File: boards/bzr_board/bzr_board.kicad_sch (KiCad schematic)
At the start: 13 parts, among them J1 Conn_01x06, U1 74HC00

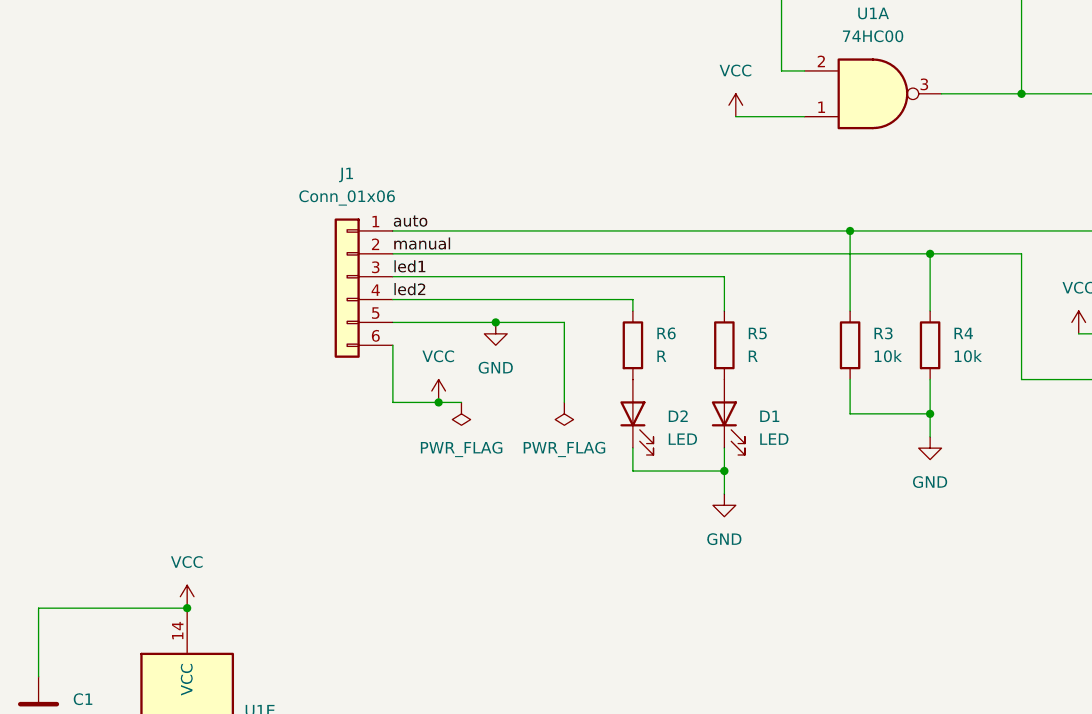
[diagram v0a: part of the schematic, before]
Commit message: set LED and resistors
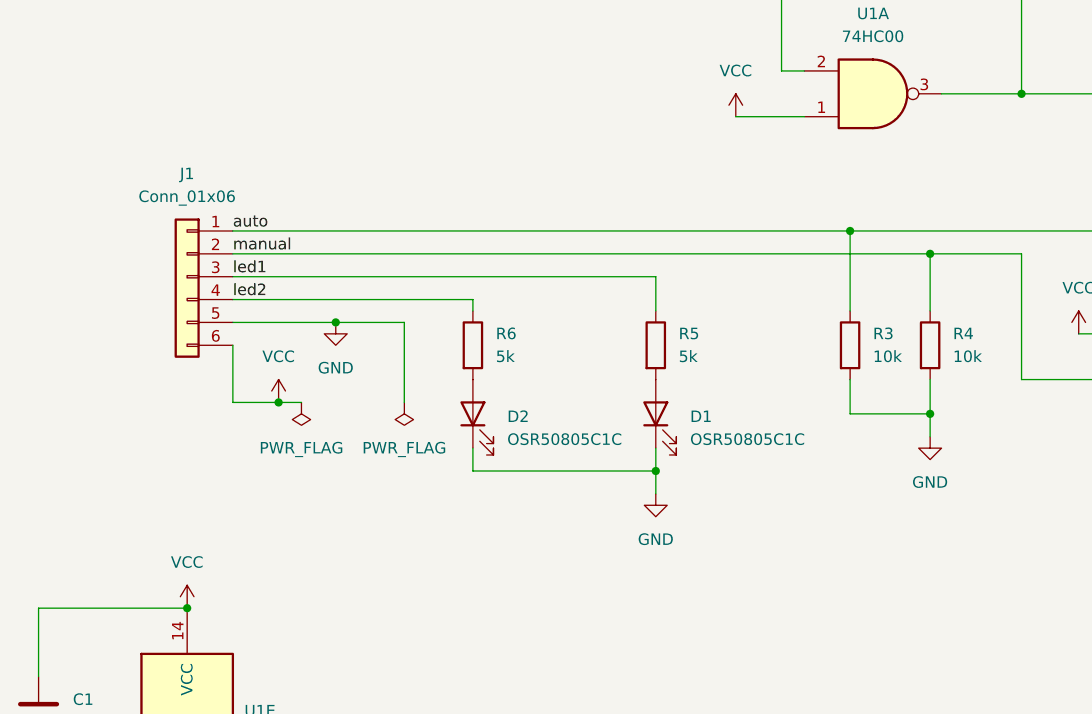
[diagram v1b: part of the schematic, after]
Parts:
- D1, D2: value LED -> OSR50805C1C
- R5, R6: value R -> 5k
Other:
- moved on the sheet: D1, D2, J1, R5, R6

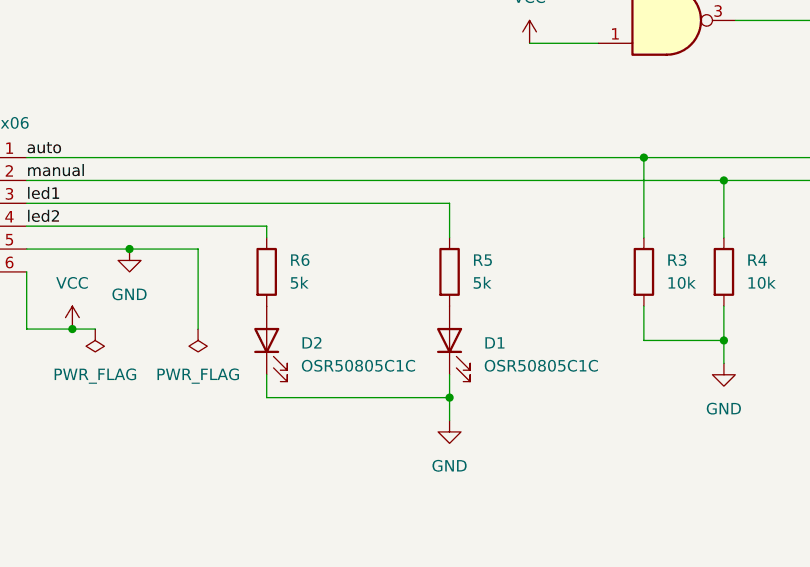
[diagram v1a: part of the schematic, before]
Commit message: change values according to actual parts
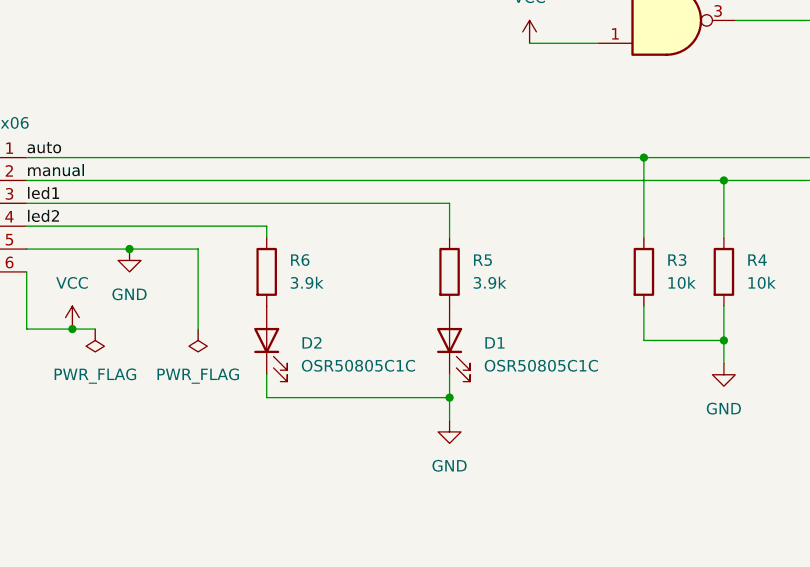
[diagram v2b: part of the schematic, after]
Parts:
- R5, R6: value 5k -> 3.9k
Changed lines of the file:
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@@
       (effects (font (size 1.27 1.27)) (justify left))
     )
-    (property "Value" "5k" (id 1) (at 100.33 83.8199 0)
+    (property "Value" "3.9k" (id 1) (at 100.33 83.8199 0)
       (effects (font (size 1.27 1.27)) (justify left))
     )
@@
       (effects (font (size 1.27 1.27)) (justify left))
     )
-    (property "Value" "5k" (id 1) (at 80.01 83.8199 0)
+    (property "Value" "3.9k" (id 1) (at 80.01 83.8199 0)
       (effects (font (size 1.27 1.27)) (justify left))
     )
@@
     )
     (path "/cf7b4bcc-23fc-4bcf-ac96-88392da5952e"
-      (reference "R5") (unit 1) (value "5k") (footprint "Resistor_SMD:R_0805_2012Metric_Pad1.20x1.40mm_HandSolder")
+      (reference "R5") (unit 1) (value "3.9k") (footprint "Resistor_SMD:R_0805_2012Metric_Pad1.20x1.40mm_HandSolder")
     )
     (path "/daa2a965-d8c0-4666-9e71-9b9e0de6b84b"
-      (reference "R6") (unit 1) (value "5k") (footprint "Resistor_SMD:R_0805_2012Metric_Pad1.20x1.40mm_HandSolder")
+      (reference "R6") (unit 1) (value "3.9k") (footprint "Resistor_SMD:R_0805_2012Metric_Pad1.20x1.40mm_HandSolder")
     )
     (path "/a6fb77b5-8aaa-4f0c-9a5f-42000d51af92"
